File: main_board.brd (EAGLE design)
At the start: 91 x 66 mm, 49 parts, among them IC1 LT1168ACS8, IC2 LT1168ACS8, IC3 LT1168ACS8, IC4 317EMP, U1 TLC272IP, U2 TLC272IP, U3 TLC272IP

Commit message: Re-doing main board. Use this
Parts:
- moved TM6 87.8 mm to (106.7, 21.6)
- moved IC3 85.2 mm to (128.3, 14.0)
- moved TM7 80.8 mm to (106.7, 10.2)
- moved PAD30 71.1 mm to (85.1, 54.6)
- moved TM5 68.5 mm to (67.3, 8.89)
- moved U3 68.0 mm to (121.9, 10.2)
- moved PAD12 67.1 mm to (77.5, 50.8)
- moved PAD11 61.5 mm to (77.5, 54.6)
- moved PAD29 61.0 mm to (39.4, 50.8)
- moved IC2 57.2 mm to (90.2, 15.2)
- moved PAD6 55.9 mm to (39.4, 54.6)
- moved PAD27 55.7 mm to (54.6, 50.8)
- moved PAD10 54.4 mm to (85.1, 50.8)
- moved PAD2 54.3 mm to (64.8, 54.6)
- moved PAD28 51.9 mm to (47.0, 50.8)
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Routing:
- net N$27: track 196.0 -> 0.00 mm, vias 1 -> 0
- net N$25: track 180.2 -> 0.00 mm, vias 2 -> 0
- net N$3: track 175.7 -> 0.00 mm, vias 1 -> 0
- net VDD: track 164.7 -> 0.00 mm, vias 2 -> 0
- net N$2: track 159.7 -> 0.00 mm, vias 3 -> 0
- net N$24: track 143.0 -> 0.00 mm, vias 2 -> 0
- net N$22: track 130.6 -> 0.00 mm, vias 1 -> 0
- net N$5: track 128.8 -> 0.00 mm, vias 1 -> 0
- net VCC: track 120.0 -> 0.00 mm
- net N$23: track 100.3 -> 0.00 mm, vias 1 -> 0
- net N$32: track 96.3 -> 0.00 mm, vias 1 -> 0
- net N$6: track 94.3 -> 0.00 mm, vias 4 -> 0
- net N$17: track 89.1 -> 0.00 mm, vias 2 -> 0
- net N$10: track 86.3 -> 0.00 mm, vias 1 -> 0
- net N$21: track 85.3 -> 0.00 mm, vias 2 -> 0
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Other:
- board size 91 x 66 mm -> 133 x 80 mm

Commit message: Progress
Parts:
- moved R5 87.8 mm to (3.81, 24.1), turned to 90 degrees
- moved R6 84.7 mm to (3.81, 17.8), turned to 90 degrees
- moved R4 77.7 mm to (119.4, 29.2)
- moved PAD3 76.3 mm to (117.1, 5.84)
- moved R9 63.2 mm to (129.5, 29.2)
- moved PAD4 61.3 mm to (111.8, 40.6)
- moved PAD10 58.5 mm to (122.2, 5.59)
- moved R14 55.0 mm to (95.2, 27.9)
- moved PAD12 52.7 mm to (48.4, 6.86)
- moved R8 52.2 mm to (108.0, 6.35)
- moved PAD9 51.4 mm to (121.9, 40.6)
- moved PAD29 51.4 mm to (90.2, 43.2)
- moved PAD11 48.4 mm to (86.2, 6.99)
- moved PAD30 47.5 mm to (81.9, 7.24)
- moved PAD27 45.4 mm to (42.5, 6.99)
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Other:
- board size 133 x 80 mm -> 134.3 x 80 mm

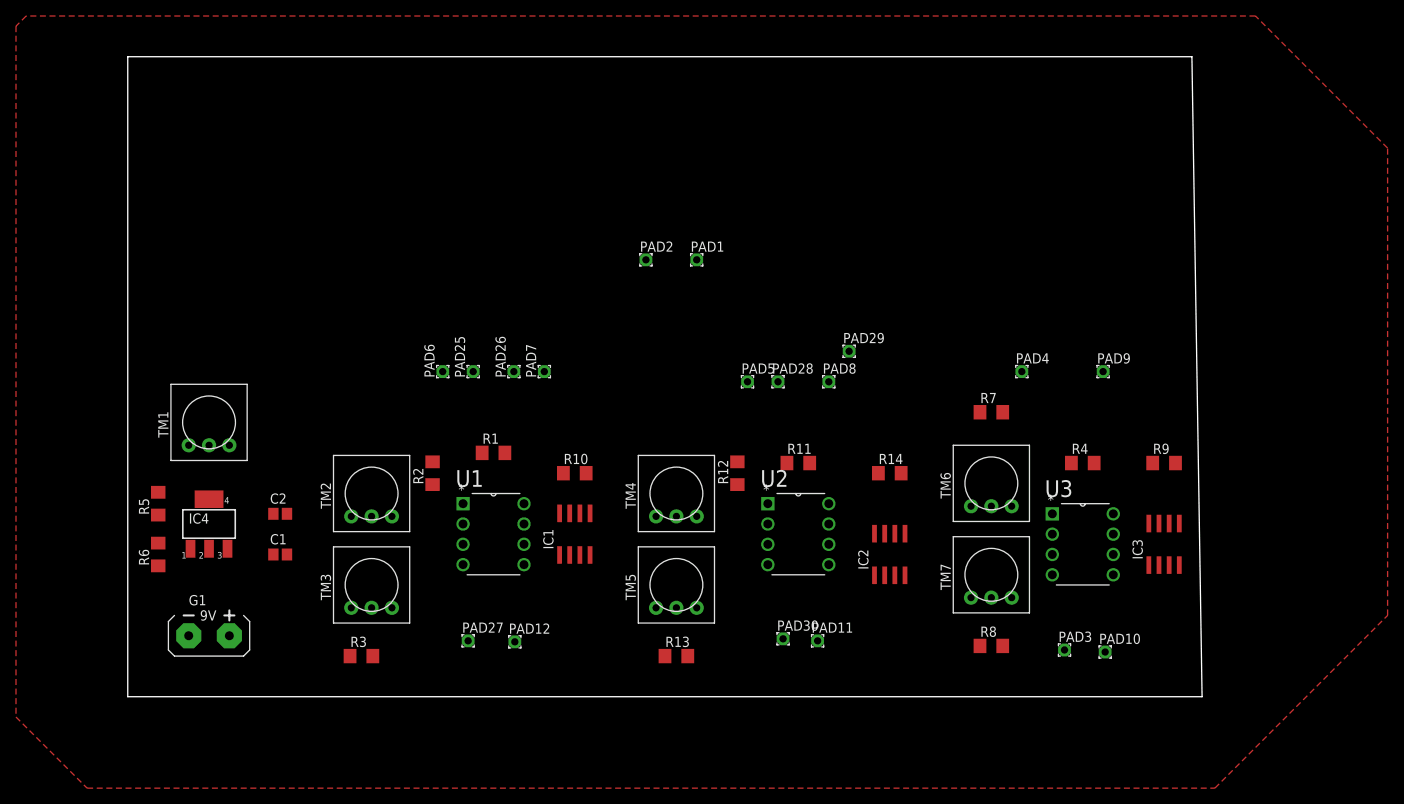
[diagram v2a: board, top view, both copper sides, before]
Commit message: Board is 100%. Left to do: text
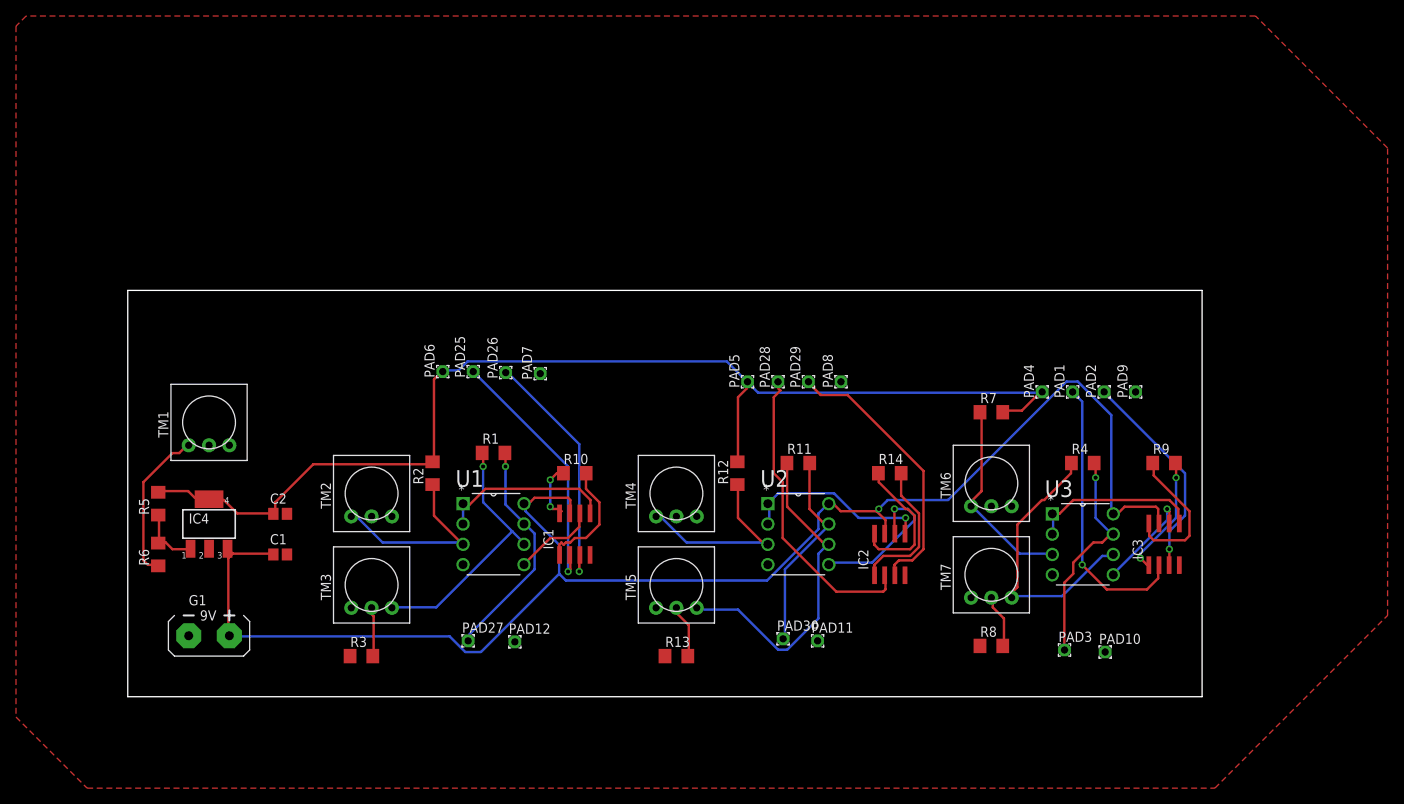
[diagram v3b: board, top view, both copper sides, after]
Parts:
- moved PAD2 59.6 mm to (122.0, 38.1), turned to 90 degrees
- moved PAD1 49.8 mm to (118.1, 38.1), turned to 90 degrees
- moved PAD29 6.35 mm to (85.1, 39.4), turned to 90 degrees
- moved PAD9 4.79 mm to (126.0, 38.1), turned to 90 degrees
- moved PAD4 3.59 mm to (114.3, 38.1), turned to 90 degrees
- moved PAD8 1.52 mm to (89.2, 39.4), turned to 90 degrees
- moved PAD26 1.02 mm to (47.2, 40.5)
- moved PAD7 0.57 mm to (51.6, 40.4)
- turned PAD28 to 90 degrees
- turned PAD5 to 90 degrees
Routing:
- net VCC: track 0.00 -> 188.4 mm, vias 0 -> 1
- net VDD: track 0.00 -> 145.1 mm
- net N$24: track 0.00 -> 41.5 mm
- net N$32: track 0.00 -> 38.0 mm
- net N$18: track 0.00 -> 35.1 mm, vias 0 -> 1
- net N$8: track 0.00 -> 35.0 mm
- net N$31: track 0.00 -> 34.9 mm
- net N$2: track 0.00 -> 32.6 mm, vias 0 -> 1
- net N$22: track 0.00 -> 32.1 mm, vias 0 -> 1
- net N$21: track 0.00 -> 30.9 mm, vias 0 -> 1
- net N$1: track 0.00 -> 28.7 mm, vias 0 -> 1
- net N$7: track 0.00 -> 27.9 mm, vias 0 -> 1
- net N$17: track 0.00 -> 26.6 mm, vias 0 -> 1
- net N$23: track 0.00 -> 25.9 mm
- net N$11: track 0.00 -> 25.1 mm
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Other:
- board size 134.3 x 80 mm -> 134.3 x 50.8 mm

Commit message: Edited text on board.
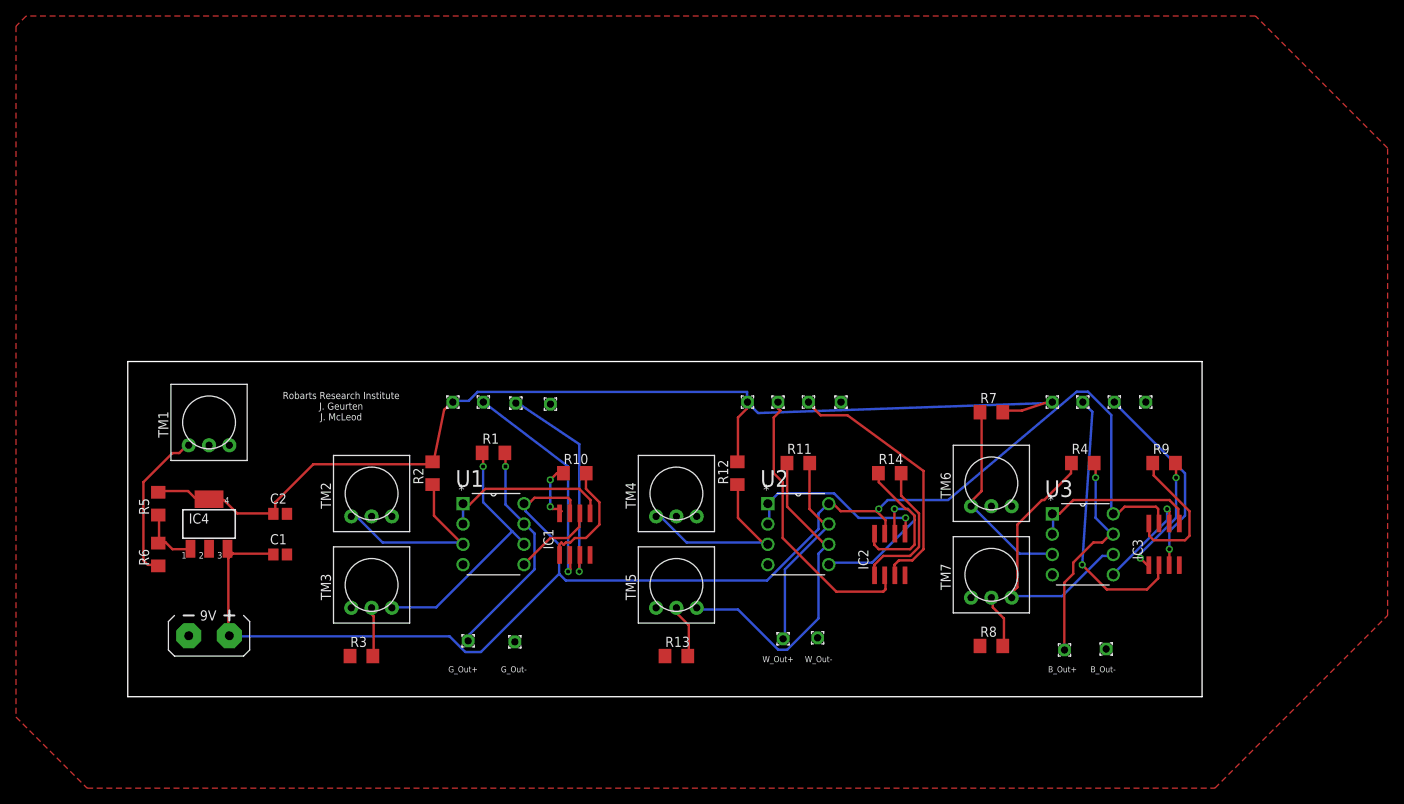
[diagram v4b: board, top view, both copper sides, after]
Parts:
- moved PAD25 4.02 mm to (44.5, 36.8)
- moved PAD6 4.02 mm to (40.6, 36.8)
- moved PAD7 4.02 mm to (52.8, 36.6)
- moved PAD26 4.02 mm to (48.5, 36.7)
- moved PAD28 2.54 mm to (81.3, 36.8)
- moved PAD29 2.54 mm to (85.1, 36.8)
- moved PAD5 2.54 mm to (77.5, 36.8)
- moved PAD8 2.54 mm to (89.2, 36.8)
- moved PAD9 1.80 mm to (127.3, 36.8)
- moved PAD1 1.80 mm to (119.4, 36.8)
- moved PAD2 1.80 mm to (123.3, 36.8)
- moved PAD4 1.80 mm to (115.6, 36.8)
- moved PAD10 0.40 mm to (122.3, 5.97)
- moved PAD11 0.38 mm to (86.2, 7.37)
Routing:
- net VDD: track 145.1 -> 139.6 mm
- net N$22: track 32.1 -> 28.6 mm
- net N$21: track 30.9 -> 27.5 mm
- net N$32: track 38.0 -> 35.5 mm
- net N$17: track 26.6 -> 24.9 mm
- net VCC: track 188.4 -> 186.6 mm
- net N$31: track 34.9 -> 33.2 mm
- net N$18: track 35.1 -> 33.9 mm
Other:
- board size 134.3 x 50.8 mm -> 134.3 x 41.9 mm
- board text added: "B_Out+"
- board text added: "B_Out-"
- board text added: "G_Out+"
- board text added: "G_Out-"
- board text added: "Robarts Research Institute J. Geurten J. McLeod"
- board text added: "W_Out+"
- board text added: "W_Out-"

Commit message: Merging
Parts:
- removed PAD1, PAD10, PAD11, PAD12, PAD2, PAD25, PAD26, PAD27, PAD28, PAD29, PAD3, PAD30, PAD4, PAD5, PAD6, PAD7, PAD8, PAD9: (no value), wirepad:1,6/0,9
- added C3, C4, C5, C6, C7: 10uF, adafruit:C2012
- added X1, X2, X3: C-GRID-04-70543, con-molex:70543-04
- added X4, X5, X6: C-GRID-02-70543, con-molex:70543-02
- C1: value (none) -> 1uF; device eagle-ltspice:C2012 -> adafruit:C2012
- C2: value (none) -> 10uF; device eagle-ltspice:C2012 -> adafruit:C2012
- R13, R7: value (none) -> 30kO
- moved C2 63.0 mm to (79.3, 41.2)
- moved R9 22.4 mm to (107.3, 31.5)
- moved R12 22.3 mm to (56.0, 37.5), turned to 0 degrees
- moved IC3 22.3 mm to (107.8, 24.1)
- moved R4 22.1 mm to (97.5, 32.5)
- moved U3 21.8 mm to (102.0, 20.6)
- moved TM6 20.7 mm to (87.6, 30.5)
- moved R7 20.6 mm to (87.5, 37.6)
- moved TM7 20.5 mm to (87.6, 17.8)
- moved R8 20.5 mm to (87.7, 9.46)
- moved R14 18.9 mm to (76.9, 32.5)
- moved IC2 18.3 mm to (78.2, 24.6)
- moved R11 16.2 mm to (68.1, 33.0)
- moved U2 16.0 mm to (72.2, 21.1)
- moved R13 14.3 mm to (55.6, 11.1)
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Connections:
- net N$11 renamed U3_1_IN+
- net N$12 renamed IC3_RG1
- net N$13 renamed TM7POT2
- net N$14 renamed IC3_RG8
- net N$15 renamed U3_2_IN+
- net N$2 renamed U1_2IN-
- net N$20 renamed U1_2IN+
- net N$24 renamed U2_2IN-
- net N$25 renamed U2_1IN+
- net N$26 renamed U2_1IN-
- net N$27 renamed TM5POT2
- net N$3 renamed U1_1IN+
- net N$30 renamed U2_2IN+
- net N$4 renamed U1_1IN-
- net N$5 renamed TM2POT2
- net N$6 renamed ADJ
- net N$8 renamed U3_2_IN-
- net N$9 renamed U3_1_IN-
- removed net N$17: IC3.3, PAD2.1
- removed net N$18: IC3.2, PAD1.1
- removed net N$21: IC1.3, PAD26.1
- removed net N$22: IC1.2, PAD25.1
- removed net N$31: IC2.3, PAD29.1
- removed net N$32: IC2.2, PAD28.1
- new net BLUE_IN_B: IC3.3, X1.2
- new net BLUE_IN_R: IC3.2, X1.3
- new net GREEN_IN_B: IC1.3, X2.2
- new net GREEN_IN_R: IC1.2, X2.3
- new net WHITE_IN_B: IC2.3, X3.2
- new net WHITE_IN_R: IC2.2, X3.3
- net GND: now also C3.2, C4.1, C5.1, C6.1, C7.2, X1.4, X2.4, X3.4, X4.2, X5.2, X6.2; no longer PAD10.1, PAD11.1, PAD12.1, PAD7.1, PAD8.1, PAD9.1
- net N$1: now also X4.1; no longer PAD27.1
- net N$23: now also X5.1; no longer PAD30.1
- net N$7: no longer PAD3.1
- net VCC: now also C4.2, C5.2, C6.2
- net VDD: now also C3.1, C7.1, X1.1, X2.1, X3.1; no longer PAD4.1, PAD5.1, PAD6.1
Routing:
- net VDD: track 139.6 -> 49.7 mm
- net WHITE_IN_R: track 0.00 -> 48.1 mm, vias 0 -> 1
- net WHITE_IN_B: track 0.00 -> 44.0 mm, vias 0 -> 1
- net BLUE_IN_R: track 0.00 -> 39.6 mm, vias 0 -> 1
- net N$32: track 35.5 -> 0.00 mm
- net N$18: track 33.9 -> 0.00 mm, vias 1 -> 0
- net N$31: track 33.2 -> 0.00 mm
- net BLUE_IN_B: track 0.00 -> 29.6 mm, vias 0 -> 1
- net N$22: track 28.6 -> 0.00 mm, vias 1 -> 0
- net N$21: track 27.5 -> 0.00 mm, vias 1 -> 0
- net N$17: track 24.9 -> 0.00 mm, vias 1 -> 0
- net N$7: track 27.9 -> 8.74 mm
- net IC3_RG8: track 18.0 -> 2.58 mm
- net IC3_RG1: track 15.2 -> 0.00 mm, vias 2 -> 0
- net N$28: track 18.0 -> 32.9 mm
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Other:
- board size 134.3 x 41.9 mm -> 112.8 x 40.5 mm
- board text removed: "B_Out+"
- board text removed: "B_Out-"
- board text removed: "G_Out+"
- board text removed: "G_Out-"
- board text removed: "Robarts Research Institute J. Geurten J. McLeod"
- board text removed: "W_Out+"
- board text removed: "W_Out-"

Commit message: Finished board
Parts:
- moved C2 19.0 mm to (60.3, 41.0), turned to 270 degrees
- moved C3 18.3 mm to (90.2, 41.1), turned to 270 degrees
- moved C7 17.7 mm to (28.5, 40.4), turned to 270 degrees
- moved R6 3.25 mm to (2.54, 16.6), turned to 270 degrees
- moved C5 3.00 mm to (78.2, 13.8)
- moved R5 2.61 mm to (3.29, 23.9)
- moved C4 2.00 mm to (45.6, 15.3)
- moved R7 1.75 mm to (85.7, 37.6), turned to 180 degrees
- moved R9 1.06 mm to (106.5, 32.3)
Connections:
- net N$1 renamed U1_2OUT
- net N$23 renamed U2_2OUT
- net N$7 renamed U3_2OUT
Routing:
- net VDD: track 49.7 -> 155.6 mm
- net GREEN_IN_R: track 0.00 -> 41.8 mm
- net GREEN_IN_B: track 0.14 -> 39.6 mm
- net IC3_RG1: track 0.00 -> 26.7 mm, vias 0 -> 2
- net VCC: track 195.1 -> 204.7 mm
- net N$28: track 32.9 -> 23.5 mm, vias 0 -> 2
- net WHITE_IN_B: track 44.0 -> 36.3 mm, vias 1 -> 0
- net WHITE_IN_R: track 48.1 -> 40.9 mm, vias 1 -> 0
- net IC3_RG8: track 2.58 -> 9.23 mm, vias 0 -> 2
- net GND: track 0.00 -> 5.79 mm, vias 0 -> 16
- net BLUE_IN_B: track 29.6 -> 34.9 mm, vias 1 -> 0
- net U2_1IN-: track 22.1 -> 25.6 mm
- net ADJ: track 9.05 -> 12.3 mm
- net U1_1IN-: track 21.6 -> 24.4 mm
- net BLUE_IN_R: track 39.6 -> 37.0 mm, vias 1 -> 0
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- added copper zone on layer 16, net GND

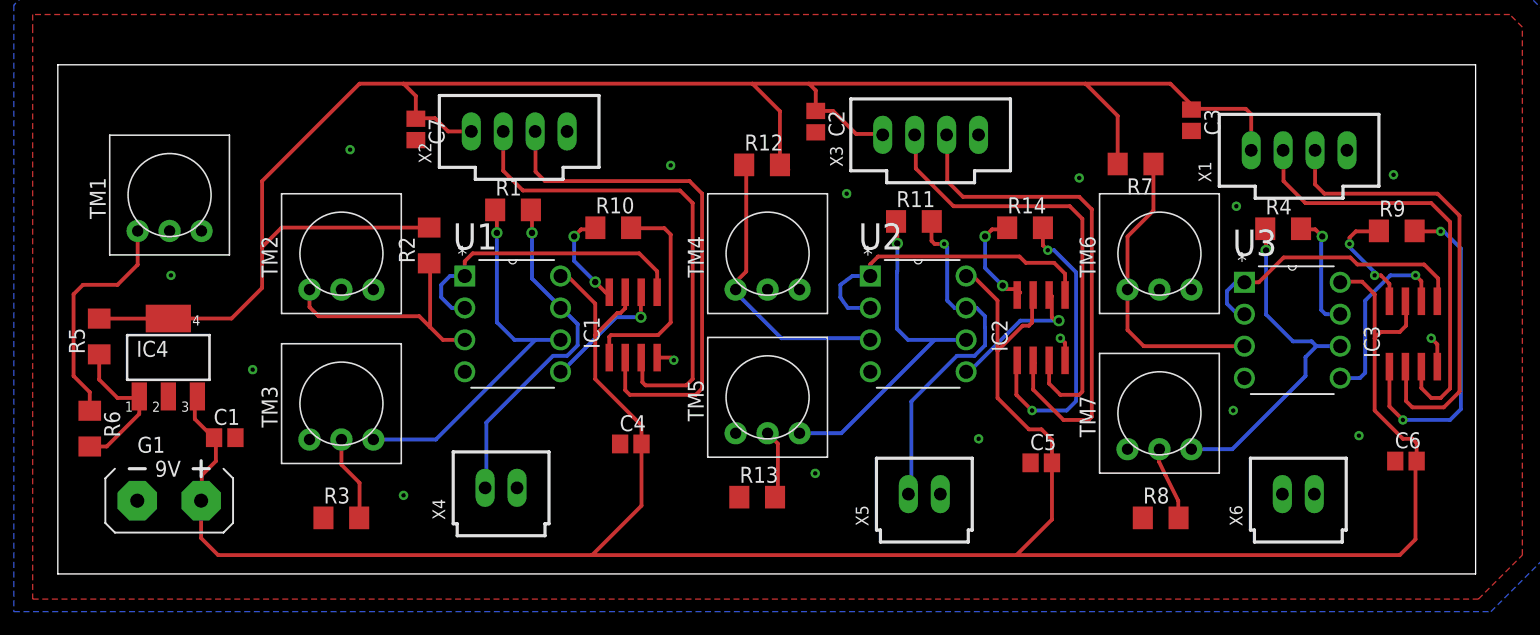
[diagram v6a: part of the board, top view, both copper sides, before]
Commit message: Finished board. No errors remaining.
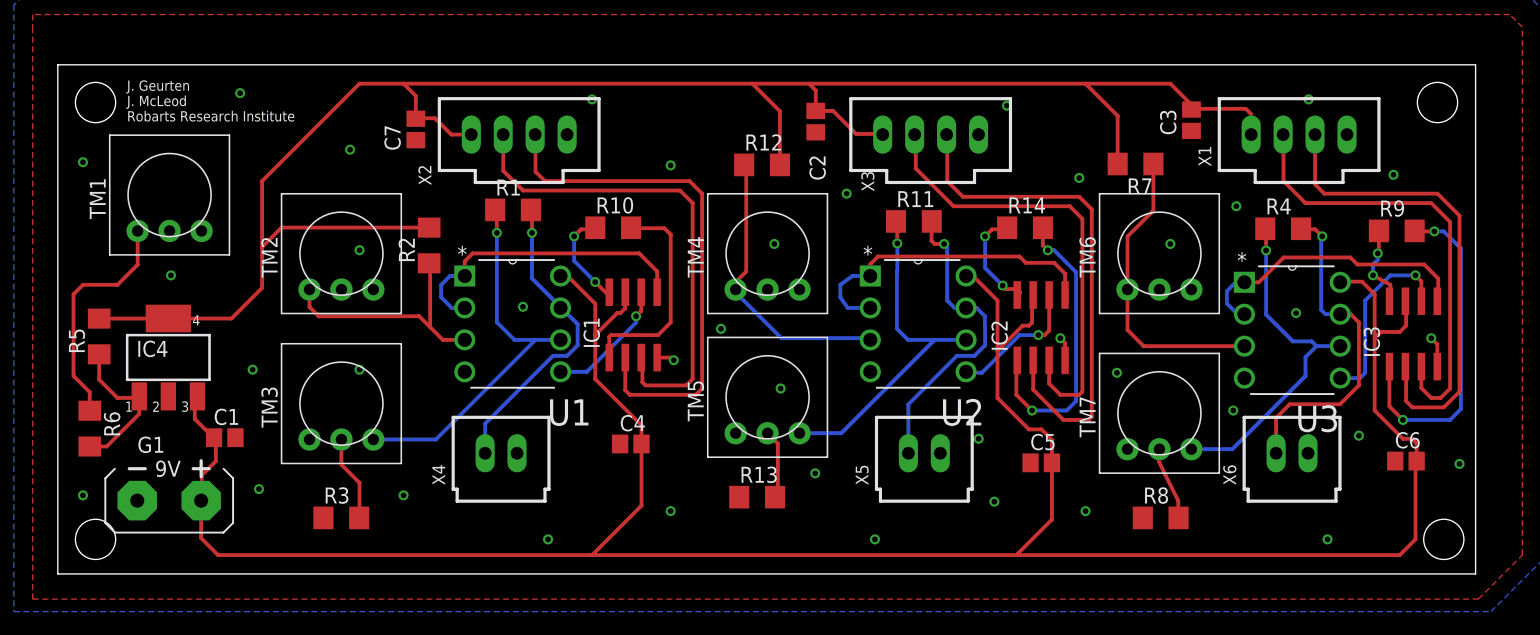
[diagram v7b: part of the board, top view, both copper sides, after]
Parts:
- moved X6 3.29 mm to (98.2, 14.6)
- moved X5 3.25 mm to (68.9, 14.6)
- moved X4 2.75 mm to (35.3, 14.6)
- moved X1 1.25 mm to (98.7, 40.0)
- moved X2 0.25 mm to (36.7, 40.0)
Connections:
- net U3_2OUT: now also X6.1
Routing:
- net U3_2OUT: track 9.50 -> 26.7 mm
- net U2_2OUT: track 28.3 -> 25.0 mm
- net U1_2OUT: track 27.3 -> 24.6 mm
- net IC3_RG8: track 9.23 -> 6.64 mm
- net BLUE_IN_R: track 37.0 -> 38.2 mm
- net BLUE_IN_B: track 34.9 -> 36.2 mm
- net VDD: track 155.6 -> 154.7 mm
- net U2_2IN+: track 11.8 -> 10.9 mm
- net GND: vias 16 -> 39
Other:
- board text added: "J. Geurten J. McLeod Robarts Research Institute"

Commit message: Finished.
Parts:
- R1, R4: value (none) -> 10kO
- R10: value (none) -> 110ohm
- R11: value (none) -> 10kO\
- R12, R2: value (none) -> 30kO
- R13: value 30kO -> 2kO
- R14, R9: value (none) -> 110 ohm
- R3, R8: value (none) -> 2kO
- R5: value (none) -> 1KO
- R6: value (none) -> 4kO
- moved G1 9.81 mm to (18.5, 9.00)
- moved R3 7.02 mm to (29.6, 8.96), turned to 180 degrees
- moved C7 1.98 mm to (26.5, 40.5)
- moved X1 1.76 mm to (100.5, 40.0)
- moved X3 1.00 mm to (70.4, 40.0)
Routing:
- net VDD: track 154.7 -> 158.9 mm
- net TM2POT2: track 6.87 -> 10.6 mm
- net VCC: track 204.7 -> 201.8 mm
- net BLUE_IN_R: track 38.2 -> 36.7 mm
- net BLUE_IN_B: track 36.2 -> 35.2 mm
- net WHITE_IN_R: track 41.0 -> 40.3 mm
